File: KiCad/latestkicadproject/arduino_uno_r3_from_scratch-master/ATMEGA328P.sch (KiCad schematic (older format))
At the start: 12 parts, among them SW1 RESET_SWITCH, U5 ATMEGA328P, X2 CSTCE16MOV53-R0

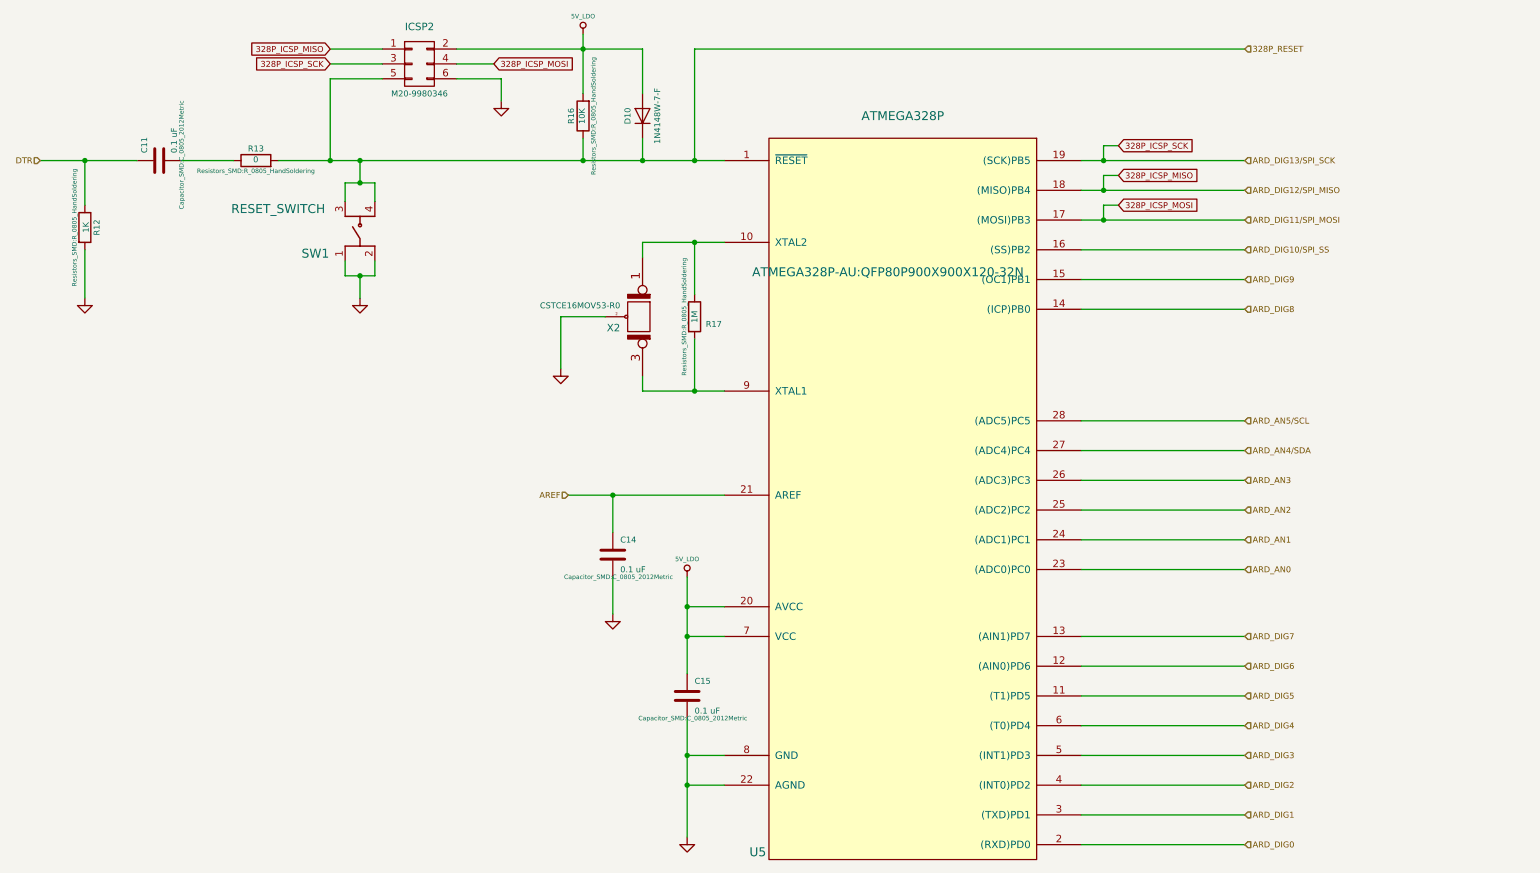
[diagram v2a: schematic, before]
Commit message: Aanpassing KiCad PCB ontwerp + footprints
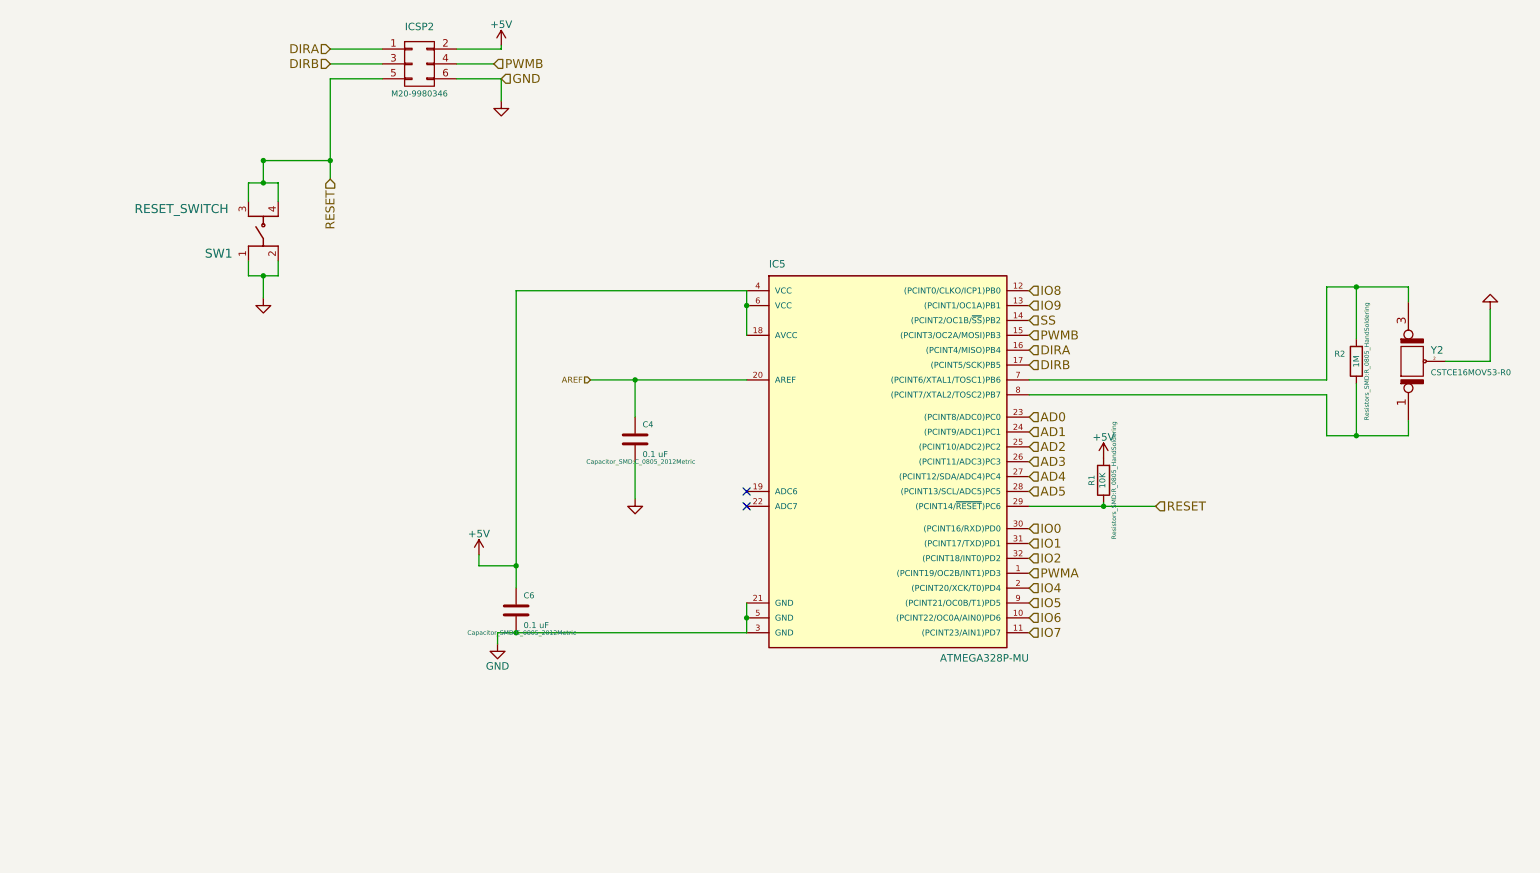
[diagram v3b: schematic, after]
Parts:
- removed C11: 0.1 uF, Capacitor_SMD:C_0805_2012Metric, symbol C
- removed D10: 1N4148W-7-F, 1N4148W-7-F:SOD3716X115N, symbol D
- removed R12: 1K, Resistors_SMD:R_0805_HandSoldering, symbol R
- removed R13: 0, Resistors_SMD:R_0805_HandSoldering, symbol R
- removed U5: ATMEGA328P, ATMEGA328P-AU:QFP80P900X900X120-32N, symbol ATMEGA328P-PU-RESCUE-Arduino_Uno_R3_From_Scratch
- added IC5: ATMEGA328P-MU, ATMEGA328P-AU:QFP80P900X900X120-32N, symbol ATMEGA328P-MU
- SW1: footprint (none) -> RESET_SWITCH:FSM4JSMATR
- renumbered C14 to C4, C15 to C6, R16 to R1, R17 to R2, X2 to Y2
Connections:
- net AREF: now also IC5.20 (AREF)
- net at R2.1, Y2.1 (P1): now also IC5.8 ((PCINT7/XTAL2/TOSC2)PB7)
- net GND: now reaches C6.2
- net GND: now also ICSP2.6 (P6), IC5.21 (GND), IC5.3 (GND), IC5.5 (GND)
- net at R2.2, Y2.3 (P3): now also IC5.7 ((PCINT6/XTAL1/TOSC1)PB6)
- net 328P_ICSP_MISO renamed DIRA
- net DIRA: now also IC5.16 ((PCINT4/MISO)PB4)
- net 328P_ICSP_MOSI renamed PWMB
- net PWMB: now also IC5.15 ((PCINT3/OC2A/MOSI)PB3)
- net 328P_ICSP_SCK renamed DIRB
- net DIRB: now also IC5.17 ((PCINT5/SCK)PB5)
- net 328P_RESET renamed RESET
- net RESET: now also IC5.29 ((PCINT14/~RESET~)PC6)
- net 5V_LDO renamed +5V
- net +5V: now also IC5.18 (AVCC), IC5.4 (VCC), IC5.6 (VCC)
- new net AD0: IC5.23 ((PCINT8/ADC0)PC0)
- new net AD1: IC5.24 ((PCINT9/ADC1)PC1)
- new net AD2: IC5.25 ((PCINT10/ADC2)PC2)
- new net AD3: IC5.26 ((PCINT11/ADC3)PC3)
- new net AD4: IC5.27 ((PCINT12/SDA/ADC4)PC4)
- new net AD5: IC5.28 ((PCINT13/SCL/ADC5)PC5)
- new net IO0: IC5.30 ((PCINT16/RXD)PD0)
- new net IO1: IC5.31 ((PCINT17/TXD)PD1)
- new net IO2: IC5.32 ((PCINT18/INT0)PD2)
- new net IO4: IC5.2 ((PCINT20/XCK/T0)PD4)
- new net IO5: IC5.9 ((PCINT21/OC0B/T1)PD5)
- new net IO6: IC5.10 ((PCINT22/OC0A/AIN0)PD6)
- new net IO7: IC5.11 ((PCINT23/AIN1)PD7)
- new net IO8: IC5.12 ((PCINT0/CLKO/ICP1)PB0)
- new net IO9: IC5.13 ((PCINT1/OC1A)PB1)
- new net PWMA: IC5.1 ((PCINT19/OC2B/INT1)PD3)
- new net SS: IC5.14 ((PCINT2/OC1B/~SS~)PB2)
- no-connect marks 0 -> 2
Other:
- moved on the sheet: C4, C6, R1, R2, SW1, Y2

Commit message: pcb routing
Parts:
- removed R2: 1M, Resistors_SMD:R_0805_HandSoldering, symbol R
- removed Y2: CSTCE16MOV53-R0, CSTCE16M0V53-R0:OSC_CSTCE16M0V53-R0, symbol CERAMIC_RESONATOR
- added C5, C9: 22P, Capacitors_SMD:C_0805, symbol C
- added Y2: Crystal, MCRSD16000F183000RR:HC%2f49US-(AT49)_1, symbol Crystal
- ICSP2: footprint (none) -> M20-9980346:HDRV6W64P254_2X3_762X508X868P
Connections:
- net GND: now also C5.2, C9.1
- net at IC5.8 ((PCINT7/XTAL2/TOSC2)PB7): now also C9.2, Y2.2
- net at IC5.7 ((PCINT6/XTAL1/TOSC1)PB6): now also C5.1, Y2.1
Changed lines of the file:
@@
 LIBS:LP2985-33DBVR
 LIBS:degson
+LIBS:PHT6NQ10T_135
 EELAYER 25 0
 EELAYER END
@@
 Comment4 ""
 $EndDescr
-Wire Wire Line
-	10100 3350 10100 3000
-Connection ~ 10100 3350
-Wire Wire Line
-	10100 2700 10100 2350
-Connection ~ 10100 2350
 Text HLabel 4950 2975 0    40   Input ~ 0
 AREF
@@
 F 0 "ICSP2" H 3800 1100 50  0000 C CNN
 F 1 "M20-9980346" H 3800 650 40  0000 C CNN
-F 2 "" H 3800 850 60  0001 C CNN
+F 2 "M20-9980346:HDRV6W64P254_2X3_762X508X868P" H 3800 850 60  0001 C CNN
 F 3 "http://cdn.harwin.com/pdfs/M20-998.pdf" H 3800 850 60  0001 C CNN
 F 4 "6 CONTACT(S), MALE, STRAIGHT TWO PART BOARD CONNECTOR" H 3800 850 60  0001 C CNN "Characteristics"
@@
 	3200 950  3200 1625
 Wire Wire Line
-	10450 3350 9900 3350
-Wire Wire Line
-	10450 3350 10450 3250
-Wire Wire Line
-	10450 2450 10450 2350
-Wire Wire Line
-	10450 2350 9900 2350
-Wire Wire Line
-	11000 2850 11000 2500
+	9900 3350 10850 3350
+Wire Wire Line
+	10450 3000 10450 3350
+Wire Wire Line
+	10450 2350 10450 2700
+Wire Wire Line
+	9900 2350 10825 2350
 $Comp
 L C C4
@@
 	-1   0    0    1
 $EndComp
-$Comp
-L R R2
-U 1 1 5615BCD3
-P 10100 2850
-F 0 "R2" H 10175 2800 40  0000 L CNN
-F 1 "1M" V 10100 2850 40  0000 C CNN
-F 2 "Resistors_SMD:R_0805_HandSoldering" V 10030 2850 30  0000 C CNN
-F 3 "http://www.vishay.com/docs/20035/dcrcwe3.pdf" H 10100 2850 30  0001 C CNN
-F 4 "RES SMD 1M OHM 1% 1/8W 0805" H 10100 2850 60  0001 C CNN "Characteristics"
-F 5 "ATMEGA328P Xtal 1M Feedback Resistor" H 10100 2850 60  0001 C CNN "Description"
-F 6 "Vishay" H 10100 2850 60  0001 C CNN "MFN"
-F 7 "CRCW08051M00FKEA" H 10100 2850 60  0001 C CNN "MFP"
-F 8 "SMD_0805" H 10100 2850 60  0001 C CNN "Package ID"
-F 9 "ANY" H 10100 2850 60  0001 C CNN "Source"
-F 10 "N" H 10100 2850 60  0001 C CNN "Critical"
-F 11 "328P_Sub" H 10100 2850 60  0001 C CNN "Subsystem"
-F 12 "~" H 10100 2850 60  0001 C CNN "Notes"
-	1    10100 2850
-	-1   0    0    1
-$EndComp
 Wire Wire Line
 	2850 1650 2850 1775
@@
 $Comp
 L GND-RESCUE-Arduino_Uno_R3_From_Scratch #PWR027
-U 1 1 56207870
-P 11000 2500
-F 0 "#PWR027" H 11000 2500 30  0001 C CNN
-F 1 "GND" H 11000 2430 30  0001 C CNN
-F 2 "~" H 11000 2500 60  0000 C CNN
-F 3 "~" H 11000 2500 60  0000 C CNN
-F 4 "ANY" H 11000 2500 60  0001 C CNN "Source"
-F 5 "N" H 11000 2500 60  0001 C CNN "Critical"
-F 6 "~" H 11000 2500 60  0001 C CNN "Notes"
-	1    11000 2500
-	-1   0    0    1
-$EndComp
-$Comp
-L GND-RESCUE-Arduino_Uno_R3_From_Scratch #PWR028
 U 1 1 562079B8
 P 2750 2425
-F 0 "#PWR028" H 2750 2425 30  0001 C CNN
+F 0 "#PWR027" H 2750 2425 30  0001 C CNN
 F 1 "GND" H 2750 2355 30  0001 C CNN
 F 2 "~" H 2750 2425 60  0000 C CNN
@@
 $EndComp
 $Comp
-L GND-RESCUE-Arduino_Uno_R3_From_Scratch #PWR029
+L GND-RESCUE-Arduino_Uno_R3_From_Scratch #PWR028
 U 1 1 56208C49
 P 4350 1100
-F 0 "#PWR029" H 4350 1100 30  0001 C CNN
+F 0 "#PWR028" H 4350 1100 30  0001 C CNN
 F 1 "GND" H 4350 1030 30  0001 C CNN
 F 2 "~" H 4350 1100 60  0000 C CNN
@@
 	1    0    0    -1
 $EndComp
-$Comp
-L CERAMIC_RESONATOR Y2
-U 1 1 5614A1DB
-P 10500 2850
-F 0 "Y2" V 10575 2750 50  0000 R CNN
-F 1 "CSTCE16MOV53-R0" V 10425 2750 40  0000 R CNN
-F 2 "CSTCE16M0V53-R0:OSC_CSTCE16M0V53-R0" H 10500 2850 60  0001 C CNN
-F 3 "http://www.murata.com/~/media/webrenewal/support/library/catalog/products/timingdevice/ceralock/p16e.ashx" H 10500 2850 60  0001 C CNN
-F 4 "CER RESONATOR 16.0MHZ SMD" H 10500 2850 60  0001 C CNN "Characteristics"
-F 5 "ATMEGA328P Oscillator" H 10500 2850 60  0001 C CNN "Description"
-F 6 "Murata" H 10500 2850 60  0001 C CNN "MFN"
-F 7 "CSTCE16M0V53-R0" H 10500 2850 60  0001 C CNN "MFP"
-F 8 "SMD" H 10500 2850 60  0001 C CNN "Package ID"
-F 9 "ANY" H 10500 2850 60  0001 C CNN "Source"
-F 10 "Y" H 10500 2850 60  0001 C CNN "Critical"
-F 11 "328P_Sub" H 10500 2850 60  0001 C CNN "Subsystem"
-F 12 "~" H 10500 2850 60  0001 C CNN "Notes"
-	1    10500 2850
-	0    -1   -1   0
-$EndComp
-Wire Wire Line
-	10700 2850 11000 2850
 $Comp
 L ATMEGA328P-MU IC5
@@
 Connection ~ 8400 3825
 $Comp
-L +5V #PWR030
+L +5V #PWR029
 U 1 1 5AA163DD
 P 8400 3500
-F 0 "#PWR030" H 8400 3350 50  0001 C CNN
+F 0 "#PWR029" H 8400 3350 50  0001 C CNN
 F 1 "+5V" H 8400 3640 50  0000 C CNN
 F 2 "" H 8400 3500 50  0001 C CNN
@@
 	4350 750  4350 725
 $Comp
-L +5V #PWR031
+L +5V #PWR030
 U 1 1 5AA16A11
 P 4350 725
-F 0 "#PWR031" H 4350 575 50  0001 C CNN
+F 0 "#PWR030" H 4350 575 50  0001 C CNN
 F 1 "+5V" H 4350 865 50  0000 C CNN
 F 2 "" H 4350 725 50  0001 C CNN
@@
 Connection ~ 4450 4675
 $Comp
-L GND #PWR032
+L GND #PWR031
 U 1 1 5AA16DB8
 P 4325 4750
-F 0 "#PWR032" H 4325 4500 50  0001 C CNN
+F 0 "#PWR031" H 4325 4500 50  0001 C CNN
 F 1 "GND" H 4325 4600 50  0000 C CNN
 F 2 "" H 4325 4750 50  0001 C CNN
@@
 Connection ~ 4450 4225
 $Comp
-L +5V #PWR033
+L +5V #PWR032
 U 1 1 5AA170DA
 P 4200 4150
-F 0 "#PWR033" H 4200 4000 50  0001 C CNN
+F 0 "#PWR032" H 4200 4000 50  0001 C CNN
 F 1 "+5V" H 4200 4290 50  0000 C CNN
 F 2 "" H 4200 4150 50  0001 C CNN
@@
 Text HLabel 4350 950  2    60   Input ~ 0
 GND
+$Comp
+L Crystal Y2
+U 1 1 5AA8FD3A
+P 10450 2850
+F 0 "Y2" H 10450 3000 50  0000 C CNN
+F 1 "Crystal" H 10450 2700 50  0000 C CNN
+F 2 "MCRSD16000F183000RR:HC%2f49US-(AT49)_1" H 10450 2850 50  0001 C CNN
+F 3 "" H 10450 2850 50  0001 C CNN
+	1    10450 2850
+	0    1    1    0
+$EndComp
+Wire Wire Line
+	10825 2350 10825 2450
+Connection ~ 10450 2350
+Wire Wire Line
+	10850 3350 10850 3250
+Connection ~ 10450 3350
+$Comp
+L C C5
+U 1 1 5AA90017
+P 10825 2600
+F 0 "C5" H 10850 2700 50  0000 L CNN
+F 1 "22P" H 10850 2500 50  0000 L CNN
+F 2 "Capacitors_SMD:C_0805" H 10863 2450 50  0001 C CNN
+F 3 "" H 10825 2600 50  0001 C CNN
+	1    10825 2600
+	1    0    0    -1
+$EndComp
+$Comp
+L C C9
+U 1 1 5AA90084
+P 10850 3100
+F 0 "C9" H 10875 3200 50  0000 L CNN
+F 1 "22P" H 10875 3000 50  0000 L CNN
+F 2 "Capacitors_SMD:C_0805" H 10888 2950 50  0001 C CNN
+F 3 "" H 10850 3100 50  0001 C CNN
+	1    10850 3100
+	1    0    0    -1
+$EndComp
+$Comp
+L GND #PWR033
+U 1 1 5AA900E3
+P 10825 2750
+F 0 "#PWR033" H 10825 2500 50  0001 C CNN
+F 1 "GND" H 10825 2600 50  0000 C CNN
+F 2 "" H 10825 2750 50  0001 C CNN
+F 3 "" H 10825 2750 50  0001 C CNN
+	1    10825 2750
+	0    -1   -1   0
+$EndComp
+$Comp
+L GND #PWR034
+U 1 1 5AA90124
+P 10850 2950
+F 0 "#PWR034" H 10850 2700 50  0001 C CNN
+F 1 "GND" H 10850 2800 50  0000 C CNN
+F 2 "" H 10850 2950 50  0001 C CNN
+F 3 "" H 10850 2950 50  0001 C CNN
+	1    10850 2950
+	0    -1   -1   0
+$EndComp
 $EndSCHEMATC
